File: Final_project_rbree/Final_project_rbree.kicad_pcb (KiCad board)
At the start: 2 copper layers, 99.1 x 99.1 mm, 48 parts, among them J1 Conn_01x02_Pin, J2 Conn_01x02_Pin, Q1 MMBT3904, Q2 AO3401A, U1 TL431, U2 LTV-817, U3 B1212, U4 2N7002, U7 NE555

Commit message: First version
First version, completed design
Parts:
- moved C4 104.6 mm to (138.5, 121.4), turned to -90 degrees
- moved R13 95.5 mm to (147.5, 104.5), turned to 90 degrees
- moved U3 89.7 mm to (155.0, 137.0), turned to -90 degrees
- moved C5 82.4 mm to (166.0, 121.1), turned to 90 degrees
- moved D2 62.4 mm to (168.5, 114.0)
- moved R16 59.4 mm to (179.6, 70.5), turned to 180 degrees
- moved R17 52.8 mm to (185.4, 70.5), turned to 180 degrees
- moved Conn_01x1 44.3 mm to (172.7, 126.0), turned to 0 degrees
- moved C6 42.4 mm to (176.5, 65.0)
- moved C7 41.4 mm to (179.4, 77.5), turned to 180 degrees
- moved C8 32.7 mm to (187.0, 75.9), turned to 90 degrees
- moved R18 27.9 mm to (174.8, 85.7), turned to -90 degrees
- moved D3 26.4 mm to (189.0, 93.0)
- moved Q2 26.4 mm to (181.7, 103.9)
- moved R19 26.4 mm to (182.4, 93.0)
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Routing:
- net VCC: track 15.0 -> 172.6 mm, vias 0 -> 2
- net GND: track 61.9 -> 117.6 mm
- net +12V: track 0.00 -> 54.5 mm, vias 0 -> 2
- net Net-(U4-D): track 6.81 -> 35.5 mm
- net Net-(U7-THR): track 0.00 -> 22.4 mm
- net /RED+: track 0.00 -> 21.2 mm
- net Net-(J1-Pin_2): track 31.7 -> 12.5 mm
- net /Vin: track 41.0 -> 27.0 mm
- net Net-(U7-Q): track 0.00 -> 13.5 mm
- net GLV+: track 0.00 -> 12.7 mm
- net Net-(U7-DIS): track 0.00 -> 11.1 mm
- net Net-(R13-Pad2): track 0.00 -> 9.85 mm
- net GLV-: track 9.79 -> 4.57 mm
- net Net-(U7-CV): track 0.00 -> 4.62 mm
- net Net-(F1-Pad1): track 7.79 -> 4.03 mm
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- added copper zone on F.Cu, net GLV-
- removed copper zone on F.Cu, net GND

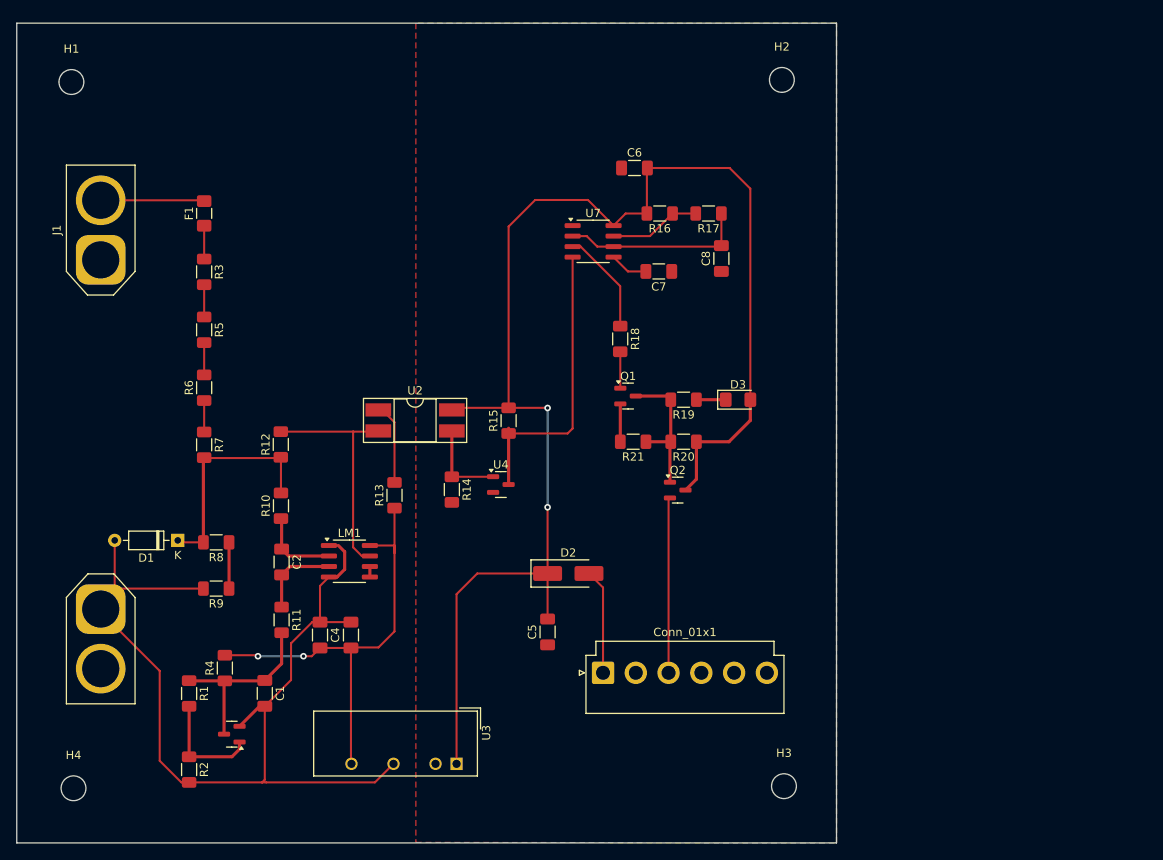
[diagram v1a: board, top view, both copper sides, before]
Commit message: PCB Redesign 1
Moved components on board to save space;
Screw holes 3mm apart;
Moved filters to better locations
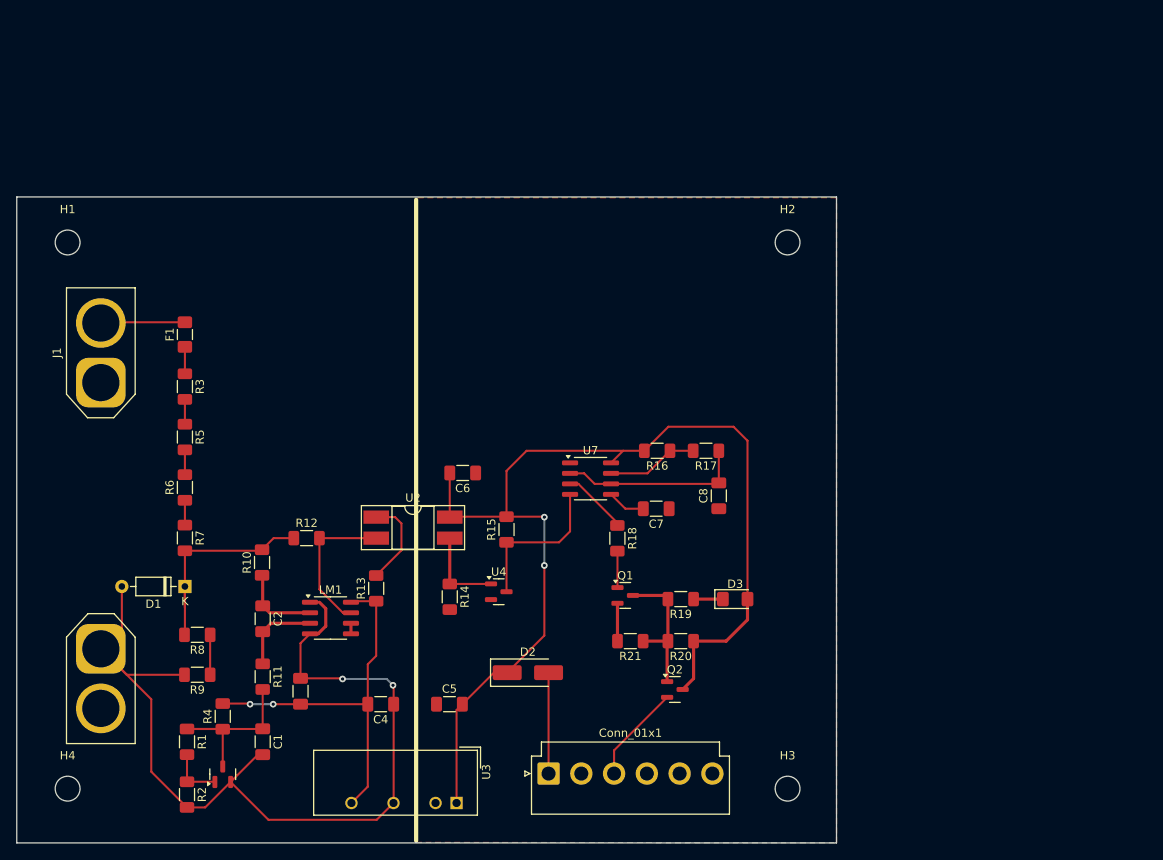
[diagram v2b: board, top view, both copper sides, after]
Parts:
- moved C6 42.3 mm to (155.7, 101.9), turned to 180 degrees
- moved U7 28.7 mm to (171.2, 102.5)
- moved C7 28.7 mm to (179.1, 106.2)
- moved C8 28.7 mm to (186.7, 104.6)
- moved R16 28.7 mm to (179.2, 99.2)
- moved R17 28.7 mm to (185.1, 99.2)
- moved R20 24.1 mm to (182.1, 122.2)
- moved R21 24.1 mm to (176.0, 122.2)
- moved D3 24.1 mm to (188.7, 117.1)
- moved Q1 24.1 mm to (175.4, 116.7)
- moved Q2 24.1 mm to (181.4, 128.0)
- moved R18 24.1 mm to (174.4, 109.7)
- moved R19 24.1 mm to (182.1, 117.1)
- moved H2 19.7 mm to (195.0, 74.0)
- moved H1 19.4 mm to (108.0, 74.0)
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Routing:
- net VCC: track 172.6 -> 131.9 mm
- net Net-(U4-D): track 35.5 -> 18.7 mm
- net Net-(LM1-Pad7): track 28.4 -> 18.0 mm
- net /RED+: track 21.2 -> 11.9 mm
- net +12V: track 54.5 -> 46.2 mm
- net Net-(U1-REF): track 13.4 -> 6.66 mm
- net Net-(U7-Q): track 13.5 -> 8.72 mm
- net Net-(J1-Pin_2): track 12.5 -> 10.2 mm
- net /Vin: track 27.0 -> 29.0 mm
- net GND: track 117.6 -> 116.0 mm, vias 0 -> 2
- net Net-(R13-Pad2): track 9.85 -> 10.9 mm
- net Net-(R5-Pad2): track 3.90 -> 3.00 mm
- net Net-(R3-Pad2): track 3.90 -> 3.00 mm
- net Net-(R6-Pad1): track 3.80 -> 3.00 mm
- net Net-(F1-Pad1): track 4.03 -> 3.25 mm
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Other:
- board size 99.1 x 99.1 mm -> 99.1 x 78.1 mm

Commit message: Added B.Cu, Silkscreen
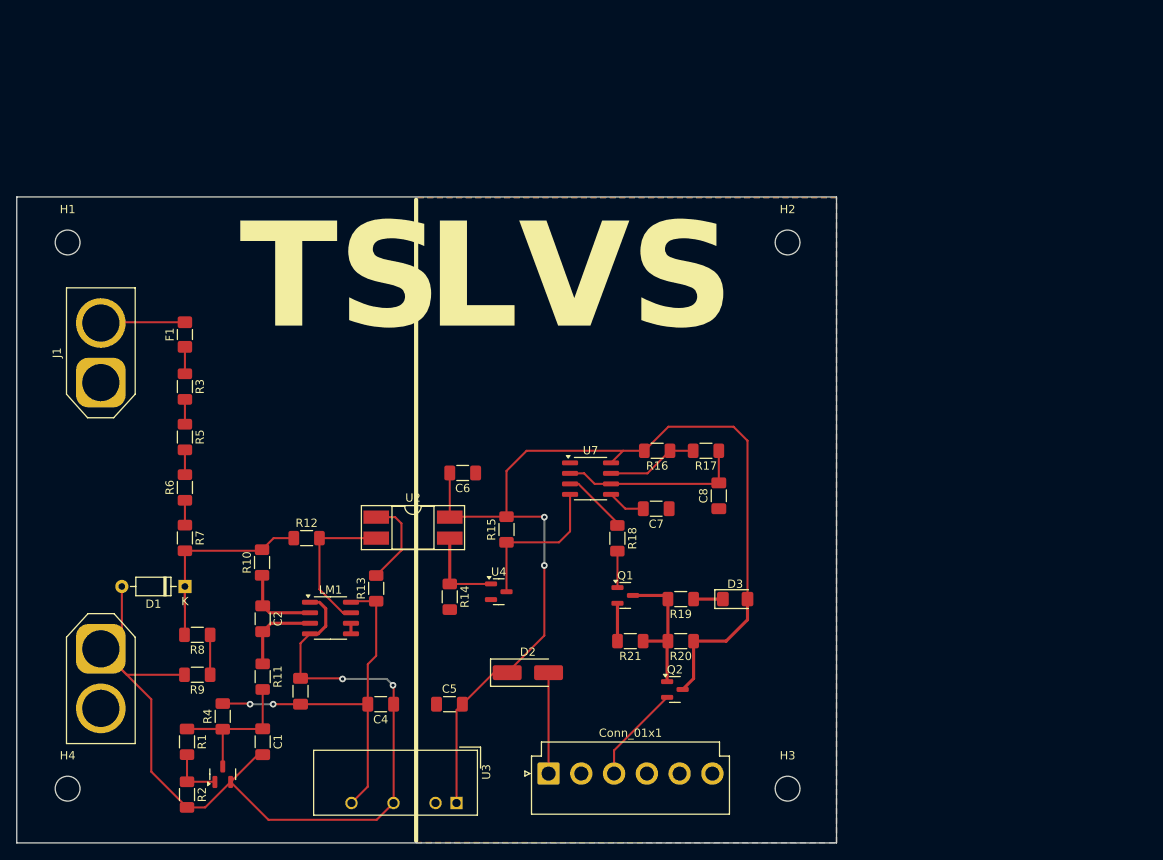
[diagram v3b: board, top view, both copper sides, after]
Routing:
- added copper zone on B.Cu, net GLV-
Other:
- board text added: "LVS"
- board text added: "TS"
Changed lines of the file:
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@@
 		(tags "Diode DO-35_SOD27 series Axial Horizontal pin pitch 7.62mm  length 4mm diameter 2mm")
 		(property "Reference" "D1"
-			(at 3.81 -2.12 360)
+			(at 3.81 -2.12 0)
 			(layer "F.SilkS")
 			(effects
@@
 		)
 		(property "Value" "12V"
-			(at 3.81 2.12 360)
+			(at 3.81 2.12 0)
 			(layer "F.Fab")
 			(effects
@@
 		)
 		(fp_text user "K"
-			(at 0 -1.8 360)
+			(at 0 -1.8 0)
 			(layer "F.SilkS")
 			(effects
@@
 		)
 		(fp_text user "${REFERENCE}"
-			(at 4.11 0 360)
+			(at 4.11 0 0)
 			(layer "F.Fab")
 			(effects
@@
 		)
 		(fp_text user "K"
-			(at 0 -1.8 360)
+			(at 0 -1.8 0)
 			(layer "F.Fab")
 			(effects
@@
 		(tags "capacitor handsolder")
 		(property "Reference" "C4"
-			(at 0 -1.85 360)
+			(at 0 -1.85 0)
 			(layer "F.SilkS")
 			(effects
@@
 		)
 		(property "Value" "1uF"
-			(at 0 1.85 360)
+			(at 0 1.85 0)
 			(layer "F.Fab")
 			(hide yes)
@@
 		)
 		(fp_text user "${REFERENCE}"
-			(at 0 0 360)
+			(at 0 0 0)
 			(layer "F.Fab")
 			(effects
@@
 		(tags "capacitor handsolder")
 		(property "Reference" "C6"
-			(at 0 -1.85 360)
+			(at 0 -1.85 0)
 			(layer "F.SilkS")
 			(effects
@@
 		)
 		(property "Value" "100n"
-			(at 0 1.85 360)
+			(at 0 1.85 0)
 			(layer "F.Fab")
 			(effects
@@
 		)
 		(fp_text user "${REFERENCE}"
-			(at 0 0 360)
+			(at 0 0 0)
 			(layer "F.Fab")
 			(effects
@@
 		(tags "capacitor handsolder")
 		(property "Reference" "C5"
-			(at 0 -1.85 360)
+			(at 0 -1.85 0)
 			(layer "F.SilkS")
 			(effects
@@
 		)
 		(property "Value" "2.2uF"
-			(at 0 1.85 360)
+			(at 0 1.85 0)
 			(layer "F.Fab")
 			(effects
@@
 		)
 		(fp_text user "${REFERENCE}"
-			(at 0 0 360)
+			(at 0 0 0)
 			(layer "F.Fab")
 			(effects
@@
 		(tags "resistor handsolder")
 		(property "Reference" "R12"
-			(at 0 -1.82 360)
+			(at 0 -1.82 0)
 			(layer "F.SilkS")
 			(effects
@@
 		)
 		(property "Value" "1M"
-			(at 0 1.82 360)
+			(at 0 1.82 0)
 			(layer "F.Fab")
 			(effects
@@
 		)
 		(fp_text user "${REFERENCE}"
-			(at 0 0 360)
+			(at 0 0 0)
 			(layer "F.Fab")
 			(effects
@@
 		(layer "Edge.Cuts")
 	)
+	(gr_text "LVS"
+		(at 151.384 85.598 0)
+		(layer "F.SilkS" knockout)
+		(effects
+			(font
+				(face "Consolas")
+				(size 12.7 12.7)
+				(thickness 0.2)
+				(bold yes)
+			)
+			(justify left bottom)
+		)
+		(render_cache "LVS" 0
+			(polygon
+				(pts
+					(xy 153.102443 83.439) (xy 153.102443 72.123326) (xy 155.283068 72.123326) (xy 155.283068 81.652314)
+					(xy 160.100294 81.652314) (xy 160.100294 83.439)
+				)
+			)
+			(polygon
+				(pts
+					(xy 167.473473 83.439) (xy 164.629045 83.439) (xy 161.148731 72.123326) (xy 163.58371 72.123326)
+					(xy 165.50998 78.938166) (xy 166.130357 81.171522) (xy 166.775549 78.807886) (xy 168.686309 72.123326)
+					(xy 170.972398 72.123326)
+				)
+			)
+			(polygon
+				(pts
+					(xy 179.812768 80.014519) (xy 179.764349 80.676093) (xy 179.602618 81.316008) (xy 179.468459 81.627499)
+					(xy 179.114347 82.18161) (xy 178.654553 82.644287) (xy 178.503773 82.759687) (xy 177.96081 83.082716)
+					(xy 177.340033 83.331003) (xy 177.027276 83.420388) (xy 176.365266 83.552703) (xy 175.719338 83.620345)
+					(xy 175.163043 83.63752) (xy 174.497108 83.624434) (xy 173.84862 83.585176) (xy 173.425988 83.544464)
+					(xy 172.800474 83.459549) (xy 172.180194 83.339739) (xy 171.769582 83.240479) (xy 171.769582 81.056752)
+					(xy 172.38899 81.234141) (xy 172.603989 81.289394) (xy 173.234305 81.431035) (xy 173.481822 81.478609)
+					(xy 174.113392 81.576915) (xy 174.359655 81.605786) (xy 175.000001 81.649406) (xy 175.20647 81.652314)
+					(xy 175.833511 81.621889) (xy 176.242499 81.556156) (xy 176.833663 81.352801) (xy 176.940423 81.292496)
+					(xy 177.33126 80.889251) (xy 177.455336 80.371236) (xy 177.28309 79.764778) (xy 177.213389 79.673312)
+					(xy 176.722879 79.259671) (xy 176.580605 79.177011) (xy 176.019539 78.910727) (xy 175.687262 78.786173)
+					(xy 175.086566 78.57115) (xy 174.666742 78.413947) (xy 174.088883 78.173927) (xy 173.646222 77.964174)
+					(xy 173.090361 77.623164) (xy 172.752879 77.340695) (xy 172.34125 76.845784) (xy 172.120095 76.450454)
+					(xy 171.933731 75.842955) (xy 171.88125 75.206599) (xy 171.942512 74.55753) (xy 172.126299 73.944132)
+					(xy 172.440365 73.383467) (xy 172.892464 72.898797) (xy 173.407559 72.542989) (xy 173.986869 72.275327)
+					(xy 174.23558 72.188466) (xy 174.840657 72.038354) (xy 175.460064 71.955961) (xy 176.145508 71.925063)
+					(xy 176.217684 71.924806) (xy 176.85905 71.940091) (xy 176.928016 71.943417) (xy 177.569912 71.980058)
+					(xy 177.66006 71.986843) (xy 178.294926 72.042011) (xy 178.357984 72.048881) (xy 178.975259 72.123326)
+					(xy 178.975259 74.108532) (xy 178.364188 73.950336) (xy 177.744783 73.836311) (xy 177.678672 73.82626)
+					(xy 177.057471 73.749925) (xy 176.96834 73.74251) (xy 176.347267 73.711763) (xy 176.285926 73.711491)
+					(xy 175.646889 73.749053) (xy 175.327443 73.807649) (xy 174.744919 74.02512) (xy 174.67915 74.065106)
+					(xy 174.313127 74.471452) (xy 174.201459 75.008078) (xy 174.42561 75.603152) (xy 174.440304 75.61915)
+					(xy 174.935855 75.999712) (xy 175.079293 76.078228) (xy 175.644493 76.334906) (xy 175.975737 76.45976)
+					(xy 176.58121 76.679561) (xy 177.005563 76.841292) (xy 177.592473 77.086765) (xy 178.035388 77.303473)
+					(xy 178.567337 77.631933) (xy 178.934935 77.936257) (xy 179.350651 78.426391) (xy 179.570821 78.817192)
+					(xy 179.766458 79.444887)
+				)
+			)
+		)
+	)
+	(gr_text "TS"
+		(at 128.778 85.598 0)
+		(layer "F.SilkS" knockout)
+		(effects
+			(font
+				(face "Consolas")
+				(size 12.7 12.7)
+				(thickness 2.54)
+				(bold yes)
+			)
+			(justify left bottom)
+		)
+		(render_cache "TS" 0
+			(polygon
+				(pts
+					(xy 134.789451 73.910011) (xy 134.789451 83.439) (xy 132.590215 83.439) (xy 132.590215 73.910011)
+					(xy 129.466618 73.910011) (xy 129.466618 72.123326) (xy 137.913048 72.123326) (xy 137.913048 73.910011)
+				)
+			)
+			(polygon
+				(pts
+					(xy 147.442036 80.014519) (xy 147.393618 80.676093) (xy 147.231887 81.316008) (xy 147.097727 81.627499)
+					(xy 146.743616 82.18161) (xy 146.283822 82.644287) (xy 146.133041 82.759687) (xy 145.590078 83.082716)
+					(xy 144.969302 83.331003) (xy 144.656545 83.420388) (xy 143.994535 83.552703) (xy 143.348607 83.620345)
+					(xy 142.792312 83.63752) (xy 142.126376 83.624434) (xy 141.477889 83.585176) (xy 141.055257 83.544464)
+					(xy 140.429743 83.459549) (xy 139.809463 83.339739) (xy 139.398851 83.240479) (xy 139.398851 81.056752)
+					(xy 140.018258 81.234141) (xy 140.233258 81.289394) (xy 140.863573 81.431035) (xy 141.111091 81.478609)
+					(xy 141.742661 81.576915) (xy 141.988924 81.605786) (xy 142.629269 81.649406) (xy 142.835739 81.652314)
+					(xy 143.46278 81.621889) (xy 143.871768 81.556156) (xy 144.462931 81.352801) (xy 144.569692 81.292496)
+					(xy 144.960529 80.889251) (xy 145.084605 80.371236) (xy 144.912359 79.764778) (xy 144.842658 79.673312)
+					(xy 144.352148 79.259671) (xy 144.209873 79.177011) (xy 143.648808 78.910727) (xy 143.316531 78.786173)
+					(xy 142.715834 78.57115) (xy 142.296011 78.413947) (xy 141.718151 78.173927) (xy 141.275491 77.964174)
+					(xy 140.71963 77.623164) (xy 140.382148 77.340695) (xy 139.970518 76.845784) (xy 139.749364 76.450454)
+					(xy 139.562999 75.842955) (xy 139.510519 75.206599) (xy 139.571781 74.55753) (xy 139.755568 73.944132)
+					(xy 140.069633 73.383467) (xy 140.521733 72.898797) (xy 141.036827 72.542989) (xy 141.616138 72.275327)
+					(xy 141.864849 72.188466) (xy 142.469925 72.038354) (xy 143.089333 71.955961) (xy 143.774776 71.925063)
+					(xy 143.846953 71.924806) (xy 144.488319 71.940091) (xy 144.557284 71.943417) (xy 145.19918 71.980058)
+					(xy 145.289329 71.986843) (xy 145.924194 72.042011) (xy 145.987253 72.048881) (xy 146.604528 72.123326)
+					(xy 146.604528 74.108532) (xy 145.993457 73.950336) (xy 145.374052 73.836311) (xy 145.30794 73.82626)
+					(xy 144.686739 73.749925) (xy 144.597609 73.74251) (xy 143.976535 73.711763) (xy 143.915194 73.711491)
+					(xy 143.276158 73.749053) (xy 142.956712 73.807649) (xy 142.374188 74.02512) (xy 142.308418 74.065106)
+					(xy 141.942396 74.471452) (xy 141.830728 75.008078) (xy 142.054879 75.603152) (xy 142.069573 75.61915)
+					(xy 142.565123 75.999712) (xy 142.708561 76.078228) (xy 143.273762 76.334906) (xy 143.605006 76.45976)
+					(xy 144.210479 76.679561) (xy 144.634831 76.841292) (xy 145.221742 77.086765) (xy 145.664657 77.303473)
+					(xy 146.196606 77.631933) (xy 146.564203 77.936257) (xy 146.979919 78.426391) (xy 147.20009 78.817192)
+					(xy 147.395726 79.444887)
+				)
+			)
+		)
+	)
 	(segment
 		(start 127.696 139.192)
@@
 			)
 		)
+	)
+	(zone
+		(net 7)
+		(net_name "GLV-")
+		(layer "B.Cu")
+		(hatch edge 0.5)
+		(priority 1)
+		(connect_pads
+			(clearance 0.254)
+		)
+		(min_thickness 0.25)
+		(filled_areas_thickness no)
+		(fill yes
+			(thermal_gap 0.5)
+			(thermal_bridge_width 0.5)
+		)
+		(polygon
+			(pts
+				(xy 150.114 68.58) (xy 150.114 146.558) (xy 200.914 146.558) (xy 200.914 68.58)
+			)
+		)

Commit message: Post-interview build
Slightly rewired PCB, schematics still have changes to be made.
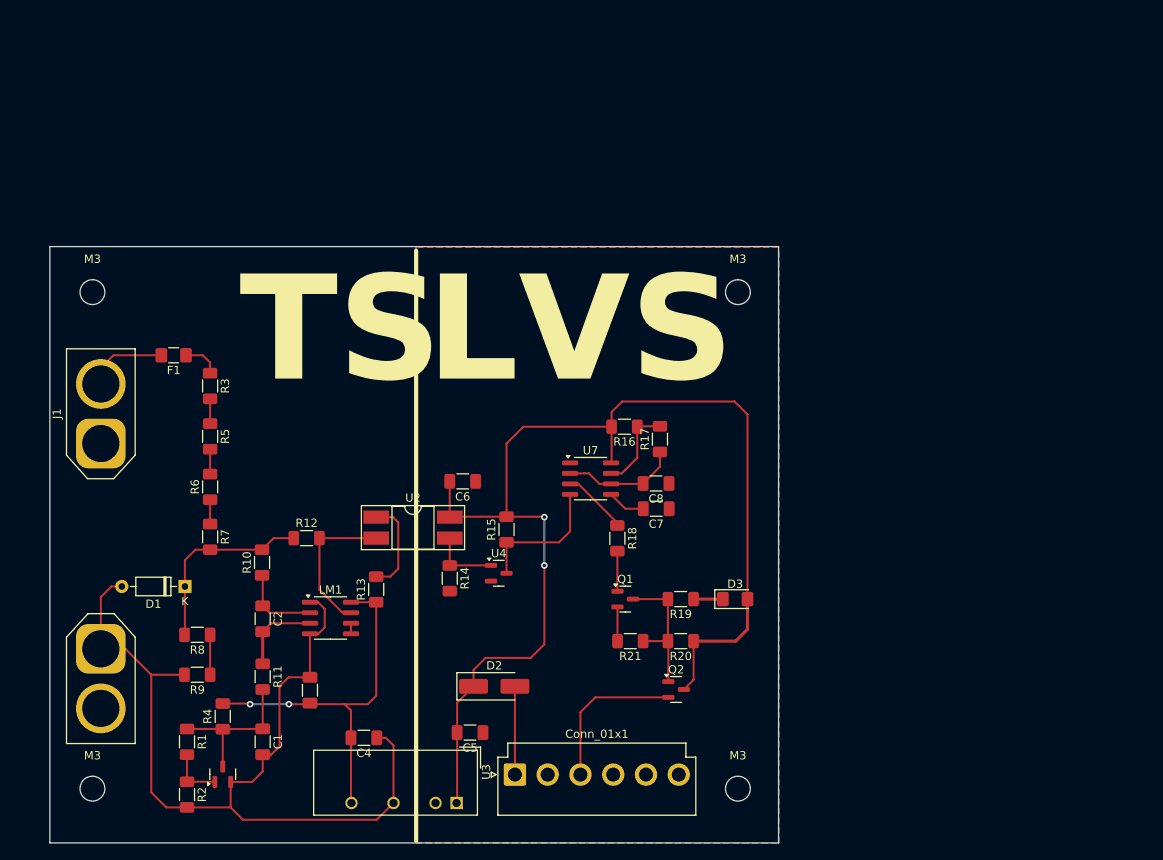
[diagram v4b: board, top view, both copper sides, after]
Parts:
- moved M3 8.49 mm to (189.0, 80.0)
- moved C8 7.73 mm to (179.1, 103.1), turned to 180 degrees
- moved J1 7.37 mm to (112.0, 98.3)
- moved M3 6.71 mm to (111.0, 80.0)
- moved M3 6.00 mm to (189.0, 140.0)
- moved R17 5.74 mm to (179.6, 97.8), turned to 90 degrees
- moved R16 4.91 mm to (175.3, 96.3)
- moved C4 4.54 mm to (143.8, 133.9)
- moved D2 4.39 mm to (159.6, 127.6)
- moved C5 4.24 mm to (156.6, 133.2), turned to 180 degrees
- moved Conn_01x1 4.07 mm to (162.1, 138.3)
- moved R7 3.05 mm to (125.2, 109.6)
- moved R3 3.05 mm to (125.2, 91.3)
- moved R5 3.05 mm to (125.2, 97.4)
- moved R6 3.05 mm to (125.2, 103.5)
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- renumbered H3 to M3, H2 to M3, H4 to M3, H1 to M3
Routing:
- net VCC: track 131.9 -> 143.5 mm
- net Net-(U7-THR): track 22.4 -> 14.0 mm
- net /RED+: track 11.9 -> 18.9 mm
- net /Vin: track 29.0 -> 23.3 mm
- net GND: track 116.0 -> 110.9 mm, vias 2 -> 0
- net Net-(U4-D): track 18.7 -> 16.4 mm
- net Net-(U4-G): track 10.5 -> 8.29 mm
- net GLV+: track 12.2 -> 10.7 mm
- net Net-(F1-Pad1): track 3.25 -> 4.56 mm
- net Net-(R13-Pad2): track 10.9 -> 11.6 mm
- net Net-(U7-DIS): track 11.1 -> 10.5 mm
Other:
- board size 99.1 x 78.1 mm -> 88.1 x 72.1 mm
